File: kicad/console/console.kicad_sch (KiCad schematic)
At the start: 3 parts, among them SW1 SW_DPST_x2

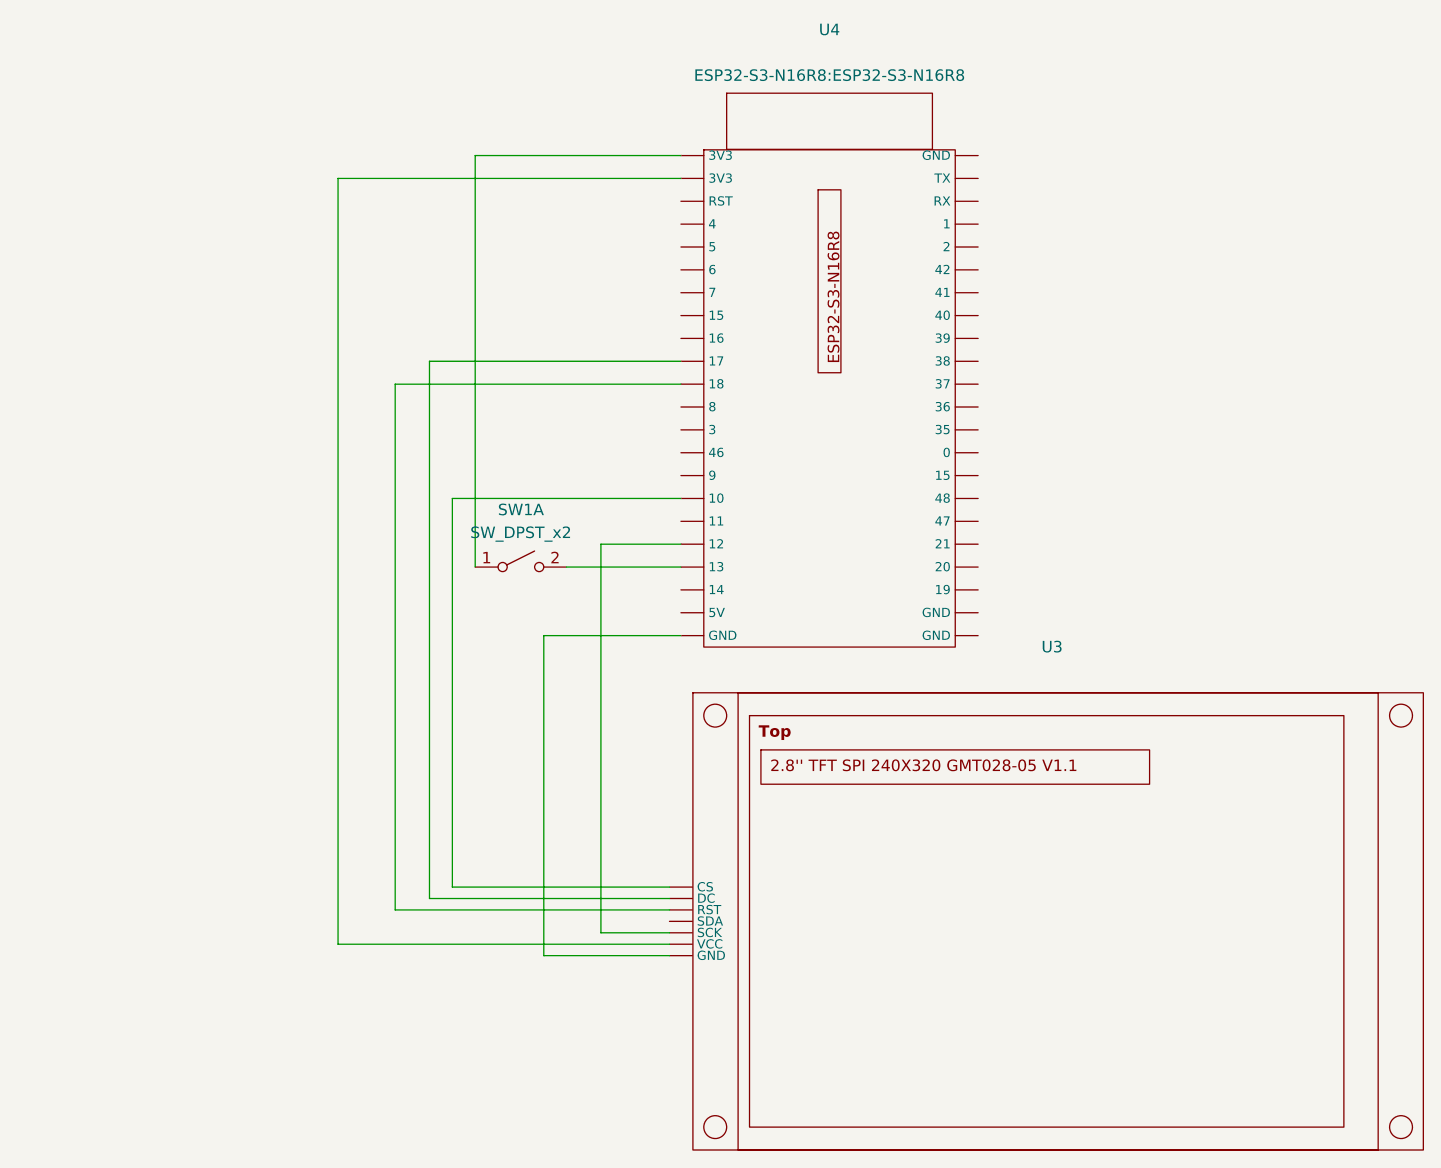
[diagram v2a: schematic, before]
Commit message: zeichnung vervollständigt. button und display sind jetzt drauf.
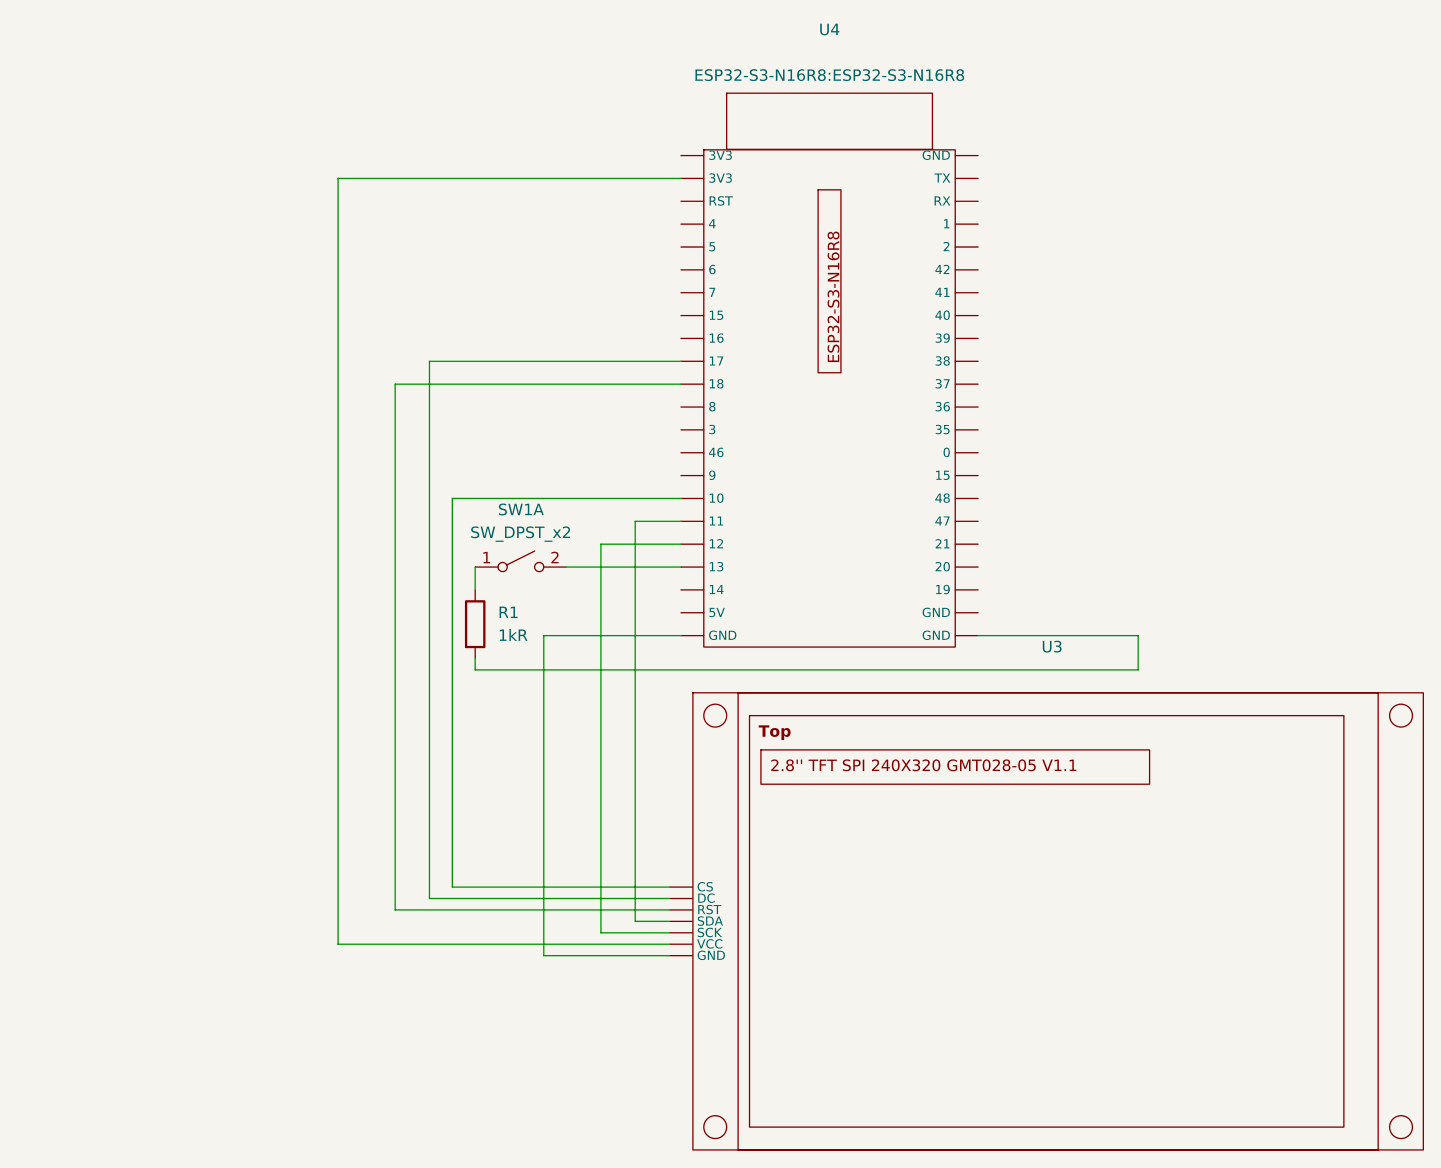
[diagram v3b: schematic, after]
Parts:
- added R1: 1kR, symbol Device:R
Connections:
- net at SW1.1 (A): now also R1.1; no longer U4. (GND)
- net at U4. (GND): now also U3. (GND)
- new net: R1.2, U4. (GND)
- new net: U3. (GND), U4. (GND) (x6)
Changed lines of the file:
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@@
+	(wire
+		(pts
+			(xy 148.59 135.89) (xy 144.78 135.89)
+		)
+		(stroke
+			(width 0)
+			(type default)
+		)
+	)
+	(wire
+		(pts
+			(xy 144.78 91.44) (xy 149.86 91.44)
+		)
+		(stroke
+			(width 0)
+			(type default)
+		)
+	)
 	(wire
 		(pts
@@
 	(wire
 		(pts
-			(xy 127 50.8) (xy 149.86 50.8)
-		)
-		(stroke
-			(width 0)
-			(type default)
-		)
-	)
-	(wire
-		(pts
 			(xy 121.92 73.66) (xy 149.86 73.66)
 		)
@@
 	(wire
 		(pts
+			(xy 200.66 107.95) (xy 200.66 104.14)
+		)
+		(stroke
+			(width 0)
+			(type default)
+		)
+	)
+	(wire
+		(pts
+			(xy 127 99.06) (xy 127 96.52)
+		)
+		(stroke
+			(width 0)
+			(type default)
+		)
+	)
+	(wire
+		(pts
 			(xy 134.62 104.14) (xy 149.86 104.14)
 		)
@@
 	(wire
 		(pts
-			(xy 127 96.52) (xy 127 50.8)
-		)
-		(stroke
-			(width 0)
-			(type default)
-		)
-	)
-	(wire
-		(pts
 			(xy 148.59 137.16) (xy 140.97 137.16)
 		)
@@
 	(wire
 		(pts
+			(xy 144.78 135.89) (xy 144.78 91.44)
+		)
+		(stroke
+			(width 0)
+			(type default)
+		)
+	)
+	(wire
+		(pts
 			(xy 118.11 76.2) (xy 118.11 134.62)
 		)
@@
 	(wire
 		(pts
+			(xy 127 107.95) (xy 127 106.68)
+		)
+		(stroke
+			(width 0)
+			(type default)
+		)
+	)
+	(wire
+		(pts
 			(xy 111.76 138.43) (xy 148.59 138.43)
 		)
@@
 	(wire
 		(pts
+			(xy 200.66 107.95) (xy 127 107.95)
+		)
+		(stroke
+			(width 0)
+			(type default)
+		)
+	)
+	(wire
+		(pts
 			(xy 124.46 88.9) (xy 149.86 88.9)
+		)
+		(stroke
+			(width 0)
+			(type default)
+		)
+	)
+	(wire
+		(pts
+			(xy 200.66 104.14) (xy 182.88 104.14)
 		)
 		(stroke
@@
 					(unit 1)
 				)
+			)
+		)
+	)
+	(symbol
+		(lib_id "Device:R")
+		(at 127 102.87 0)
+		(unit 1)
+		(exclude_from_sim no)
+		(in_bom yes)
+		(on_board yes)
+		(dnp no)
+		(fields_autoplaced yes)
+		(property "Reference" "R1"
+			(at 129.54 101.5999 0)
+			(effects
+				(font
+					(size 1.27 1.27)
+				)
+				(justify left)
+			)
+		)
+		(property "Value" "1kR"
+			(at 129.54 104.1399 0)
+			(effects
+				(font
+					(size 1.27 1.27)
+				)
+				(justify left)
+			)
+		)
+		(property "Footprint" ""
+			(at 125.222 102.87 90)
+			(effects
+				(font
+					(size 1.27 1.27)
+				)
+				(hide yes)
+			)
+		)
+		(property "Datasheet" "~"
+			(at 127 102.87 0)
+			(effects
+				(font
+					(size 1.27 1.27)
+				)
+				(hide yes)
+			)
+		)
+		(property "Description" "Resistor"
+			(at 127 102.87 0)
+			(effects
+				(font
+					(size 1.27 1.27)
+				)
+				(hide yes)
+			)
+		)
+		(pin "1"
+		)
+		(pin "2"
+		)
+		(instances
+			(project ""
+				(path "/62a2f419-179e-43b6-8483-7e1508ae9f10"
+					(reference "R1")
+					(unit 1)
+				)

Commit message: color coding und anschlüsse kontrolliert. klappt auf meinem esp :)
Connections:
- net at U4. (GND): now also U3. (GND)
- new net: U3. (GND), U4. (GND) (x6)
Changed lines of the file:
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@@
 			(width 0)
 			(type default)
+			(color 0 0 0 1)
 		)
 	)
@@
 			(width 0)
 			(type default)
+			(color 255 254 1 1)
 		)
 	)
@@
 			(width 0)
 			(type default)
+			(color 255 254 1 1)
 		)
 	)
@@
 			(width 0)
 			(type default)
+			(color 34 181 0 1)
 		)
 	)
@@
 			(width 0)
 			(type default)
+			(color 0 13 255 1)
 		)
 	)
@@
 			(width 0)
 			(type default)
+			(color 0 0 0 1)
 		)
 	)
@@
 			(width 0)
 			(type default)
+			(color 255 122 0 1)
 		)
 	)
@@
 			(width 0)
 			(type default)
+			(color 34 181 0 1)
 		)
 	)
@@
 			(width 0)
 			(type default)
+			(color 0 0 0 1)
 		)
 	)
@@
 			(width 0)
 			(type default)
+			(color 162 80 57 1)
 		)
 	)
@@
 			(width 0)
 			(type default)
+			(color 255 0 15 1)
 		)
 	)
@@
 			(width 0)
 			(type default)
+			(color 255 122 0 1)
 		)
 	)
@@
 			(width 0)
 			(type default)
+			(color 0 13 255 1)
 		)
 	)
@@
 			(width 0)
 			(type default)
+			(color 0 13 255 1)
 		)
 	)
@@
 			(width 0)
 			(type default)
+			(color 162 80 57 1)
 		)
 	)
@@
 			(width 0)
 			(type default)
+			(color 255 254 1 1)
 		)
 	)
@@
 			(width 0)
 			(type default)
+			(color 34 181 0 1)
 		)
 	)
@@
 			(width 0)
 			(type default)
+			(color 255 0 15 1)
 		)
 	)
@@
 			(width 0)
 			(type default)
+			(color 255 122 0 1)
 		)
 	)
@@
 			(width 0)
 			(type default)
+			(color 255 0 15 1)
 		)
 	)
@@
 			(width 0)
 			(type default)
-		)
-	)
+			(color 162 80 57 1)
+		)
+	)

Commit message: schaltung funktioniert
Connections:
- net at U4. (GND): now also U3. (GND)
- new net: U3. (GND), U4. (GND) (x6)
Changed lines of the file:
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@@
 			(width 0)
 			(type default)
+			(color 152 0 255 1)
 		)
 	)
@@
 			(width 0)
 			(type default)
+			(color 152 0 255 1)
 		)
 	)

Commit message: farbänderung
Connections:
- net at U4. (GND): now also U3. (GND)
- new net: U3. (GND), U4. (GND) (x6)
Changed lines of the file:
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@@
 			(width 0)
 			(type default)
+			(color 0 0 0 1)
 		)
 	)
@@
 			(width 0)
 			(type default)
+			(color 0 0 0 1)
 		)
 	)
@@
 			(width 0)
 			(type default)
+			(color 0 0 0 1)
 		)
 	)
@@
 			(width 0)
 			(type default)
-		)
-	)
+			(color 0 0 0 1)
+		)
+	)
